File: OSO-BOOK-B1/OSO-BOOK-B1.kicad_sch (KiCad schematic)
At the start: 73 parts, among them J1 USB_C_Receptacle_USB2.0, J2 Conn_01x02_MountingPin, J3 Conn_01x24, J4 Conn_01x06, J5 JST-PH3, J6 JST-PH4, J7 JST-PH3, J8 Conn_ARM_JTAG_SWD_10, Q1 DMG3415, Q2 Q_PMOS_GSD, Q3 Q_NMOS_GSD, U1 XC6220B331MR-G, U2 ESP32-S3-WROOM-1, U3 MEM2075, U4 MCP73831-2-OT, U5 R1218, Y1 32.768 kHz

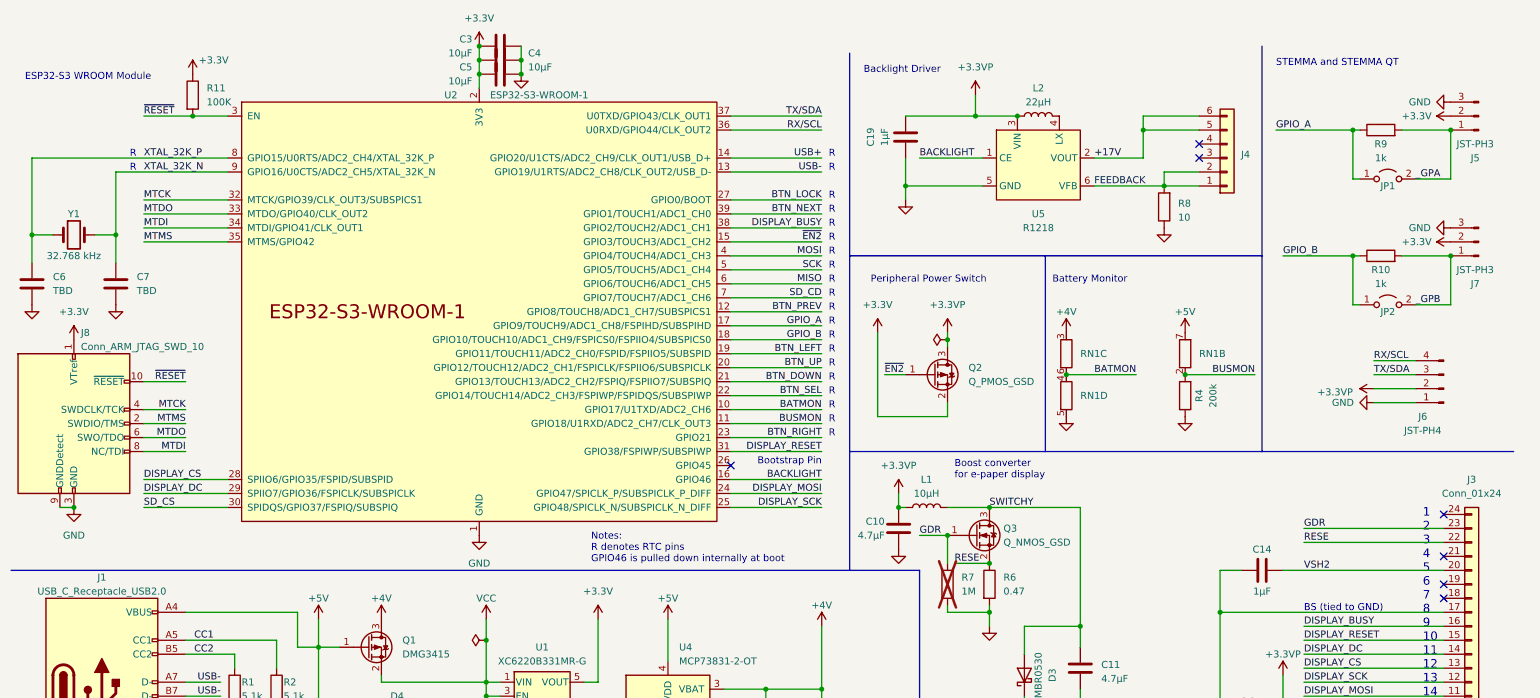
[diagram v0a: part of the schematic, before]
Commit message: Use surface mount push buttons
These buttons are basic parts at JLCPCB, so really inexpensive to use (1
cent per part, no setup fee).  They can then be covered by a silicone
cover for moisture protection and good looks.  Or even a 3d printed
cover can do the trick.
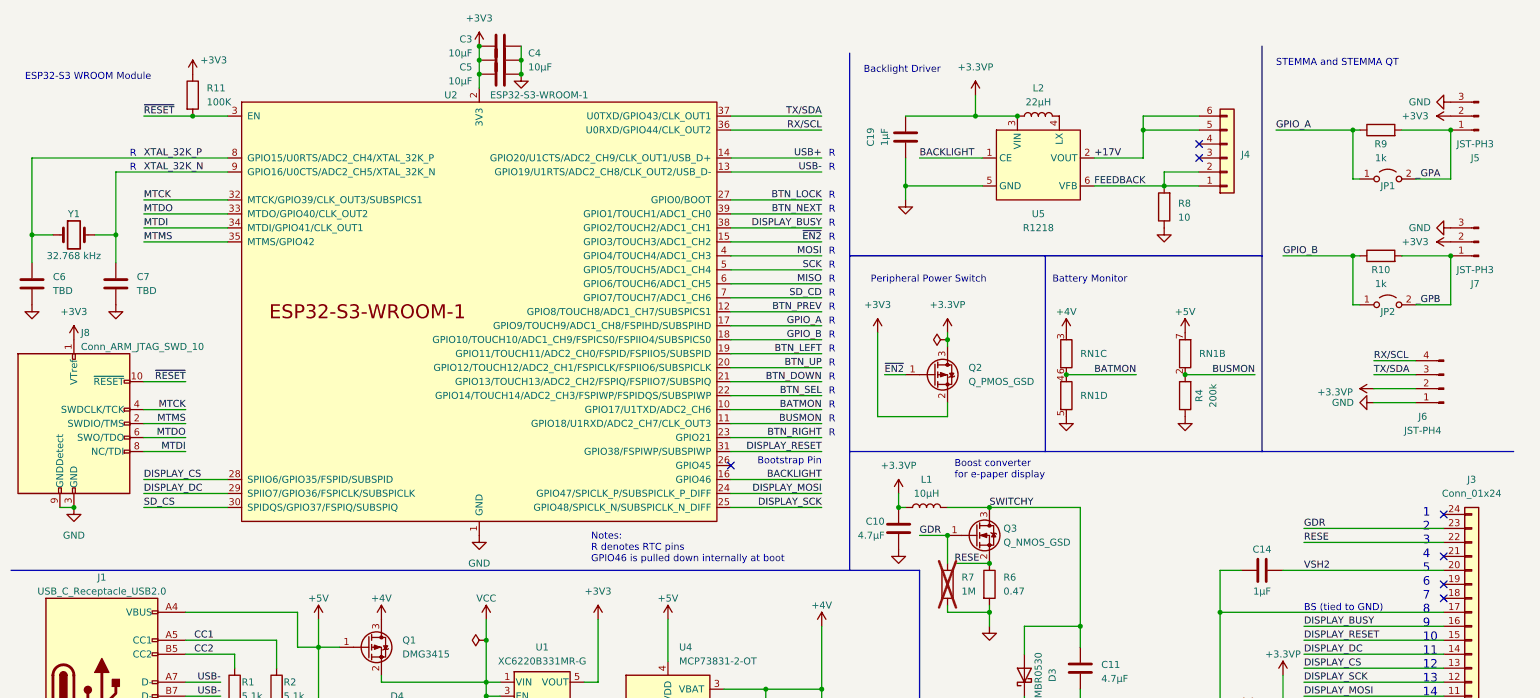
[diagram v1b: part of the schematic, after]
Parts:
- B3, B4, B5, B6, B7, B8, B9: footprint TACT_PANA-EVQ:TACT_PANA-EVQ-BUTTONPAD -> Button_Switch_SMD:SW_Push_1P1T_XKB_TS-1187A; JLCPCB (none) -> C318884
- U2: JLCPCB (none) -> C473012

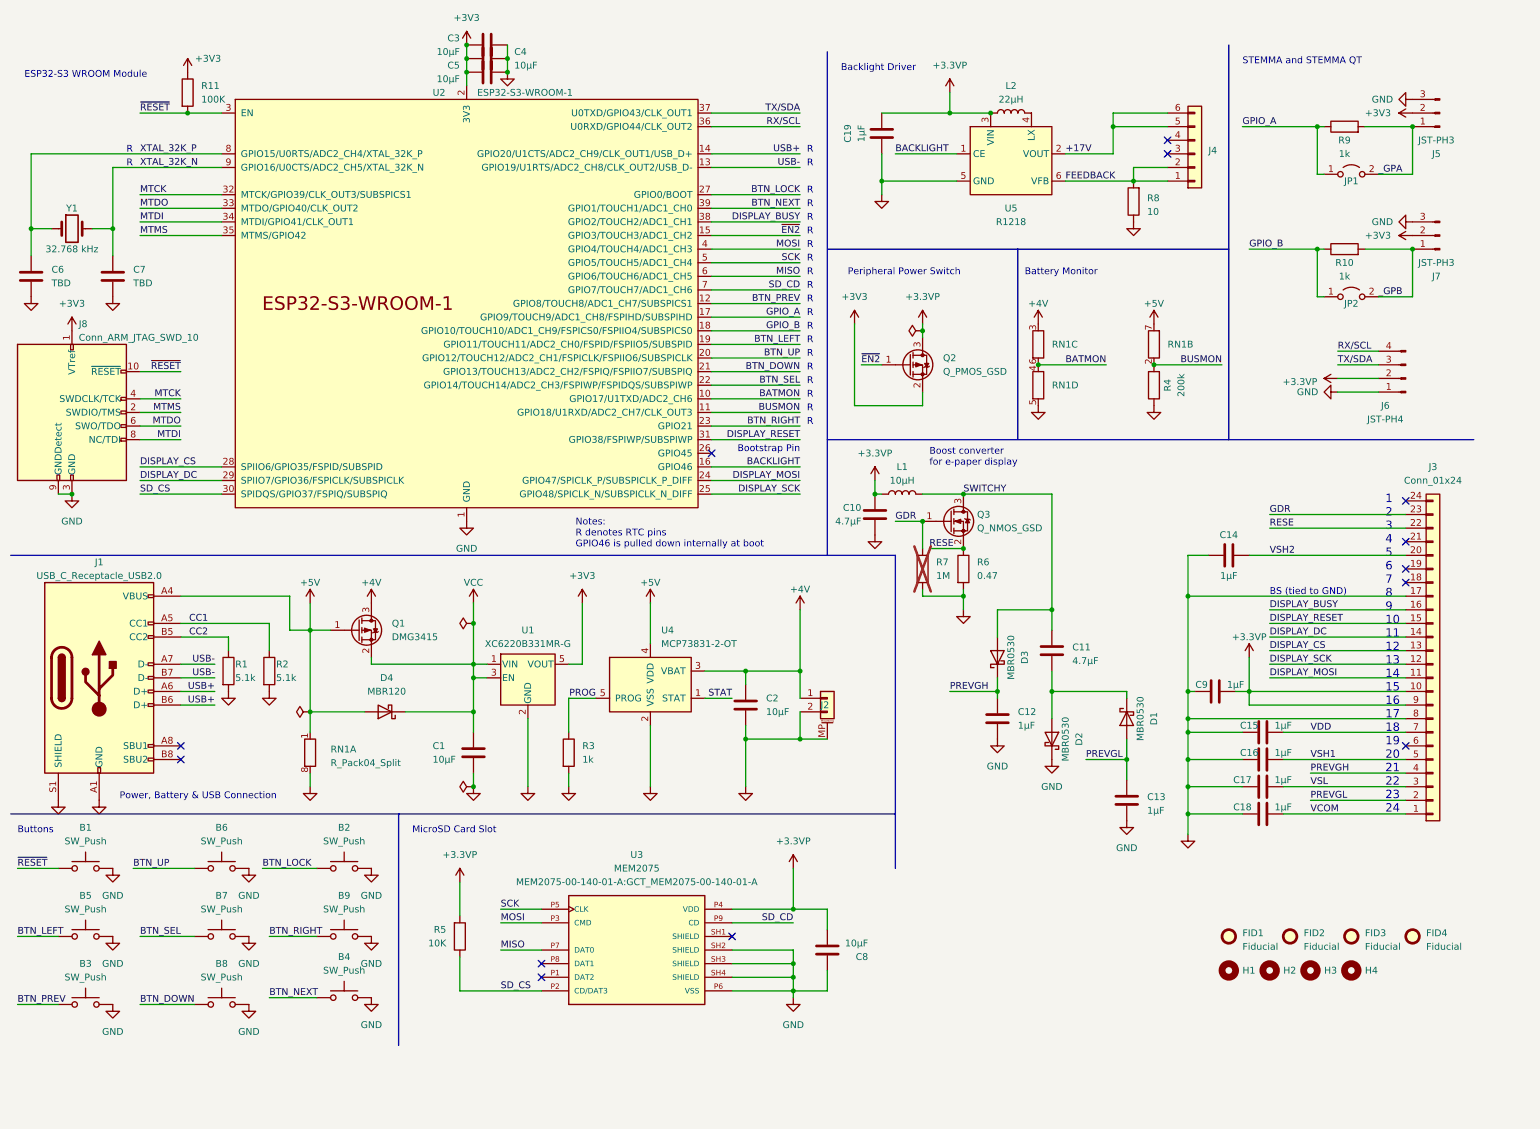
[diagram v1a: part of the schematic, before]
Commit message: Switch some parts
 - Pick a different SD-Card that is widely available
 - Use JLCPCB basic parts when possible
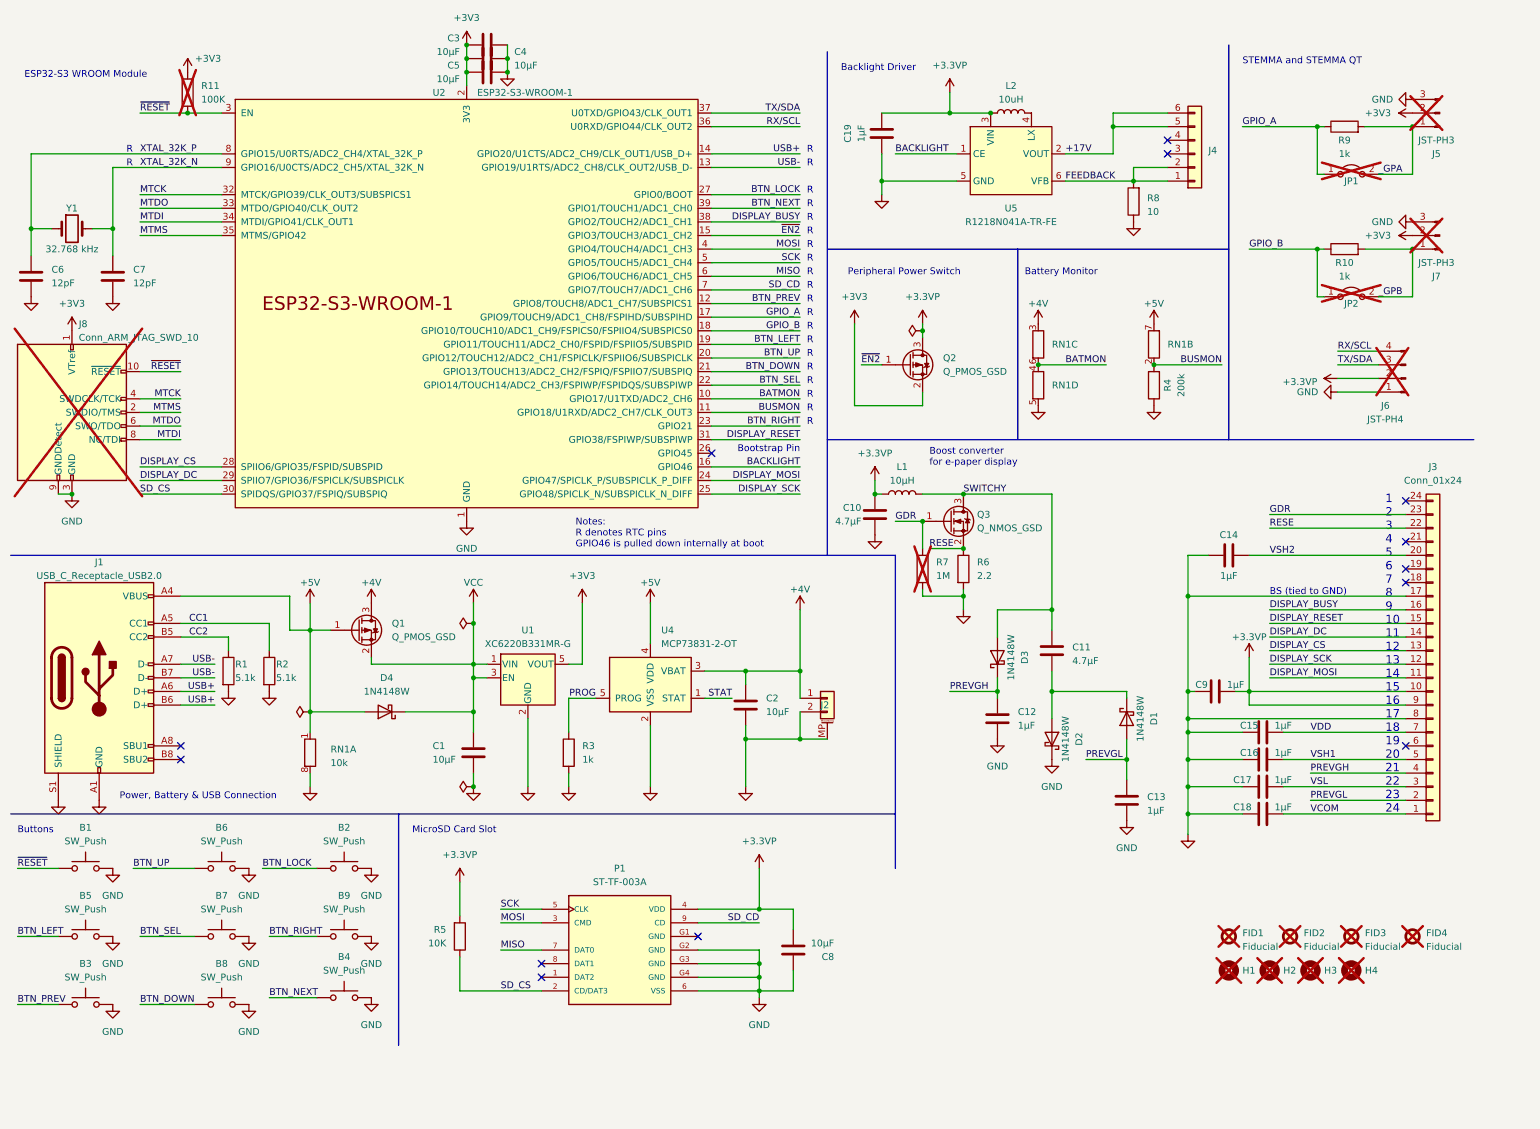
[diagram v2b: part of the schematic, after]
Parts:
- removed U3: MEM2075, MEM2075-00-140-01-A:GCT_MEM2075-00-140-01-A, symbol MEM2075-00-140-01-A:MEM2075-00-140-01-A
- added P1: ST-TF-003A, TF-CARD:SUNTECH_ST-TF-003A, symbol TF-CARD:ST-TF-003A
- B1, B2: JLCPCB (none) -> C128539
- C1, C2, C3, C4, C5, C8: JLCPCB (none) -> C13585
- C10, C11: JLCPCB (none) -> C1779
- C12, C13, C14, C15, C16, C17, C18, C19, C9: JLCPCB (none) -> C28323
- C6, C7: value TBD -> 12pF; footprint Capacitor_SMD:C_0805_2012Metric -> Capacitor_SMD:C_0603_1608Metric; JLCPCB (none) -> C38523
- D1, D2, D3: value MBR0530 -> 1N4148W; JLCPCB (none) -> C81598
- D4: value MBR120 -> 1N4148W; JLCPCB (none) -> C81598
- FID1, FID2, FID3, FID4, H1, H2, H3, H4, J5, J6, J7, J8, JP1, JP2, R11: now not fitted
- J1: JLCPCB (none) -> C165948
- J2: JLCPCB (none) -> C177225
- J3: JLCPCB (none) -> C262683
- J4: JLCPCB (none) -> C7465444
- L1: footprint Inductor_SMD:L_Taiyo-Yuden_MD-4040 -> Inductor_SMD:L_0805_2012Metric; JLCPCB (none) -> C1046
- L2: value 22µH -> 10uH; footprint Inductor_SMD:L_1210_3225Metric -> Inductor_SMD:L_0805_2012Metric; JLCPCB (none) -> C1046
- Q1: value DMG3415 -> Q_PMOS_GSD; JLCPCB (none) -> C15127
- Q2: JLCPCB (none) -> C15127
- Q3: JLCPCB (none) -> C8545
- R1, R2: JLCPCB (none) -> C27834
- R10, R3, R9: JLCPCB (none) -> C17513
- R4: JLCPCB (none) -> C17539
- R5: JLCPCB (none) -> C17414
- R6: value 0.47 -> 2.2; JLCPCB (none) -> C17521
- R8: JLCPCB (none) -> C17415
- RN1: value R_Pack04_Split -> 10k; JLCPCB (none) -> C29718
- U1: JLCPCB (none) -> C86534
- U4: JLCPCB (none) -> C424093
- U5: value R1218 -> R1218N041A-TR-FE; JLCPCB (none) -> C6749144
- Y1: JLCPCB (none) -> C32346
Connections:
- net +3.3VP: now also P1.4 (VDD)
- net GND: now also P1.6 (VSS), P1.G2 (GND), P1.G3 (GND), P1.G4 (GND)
- net MISO: now also P1.7 (DAT0)
- net MOSI: now also P1.3 (CMD)
- net SCK: now also P1.5 (CLK)
- net SD_CD: now also P1.9 (CD)
- net SD_CS: now also P1.2 (CD/DAT3)
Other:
- moved on the sheet: C8

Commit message: Packing script
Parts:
- FID1, FID2, FID3, FID4, R11: now left out of the parts list
- P1: JLCPCB (none) -> C393941
- R7: JLCPCB (none) -> C4310; now fitted

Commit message: More work on the buttons: rubber or SMD option
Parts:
- B3, B4, B5, B6, B7, B8, B9: footprint Button_Switch_SMD:SW_Push_1P1T_XKB_TS-1187A -> Keypad:SW_Push_1P1T_XKB_TS-1187A-Silicon-Hybrid
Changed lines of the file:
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@@
 			)
 		)
-		(property "Footprint" "Button_Switch_SMD:SW_Push_1P1T_XKB_TS-1187A"
+		(property "Footprint" "Keypad:SW_Push_1P1T_XKB_TS-1187A-Silicon-Hybrid"
 			(at 52.07 172.72 0)
 			(effects
@@
 			)
 		)
-		(property "Footprint" "Button_Switch_SMD:SW_Push_1P1T_XKB_TS-1187A"
+		(property "Footprint" "Keypad:SW_Push_1P1T_XKB_TS-1187A-Silicon-Hybrid"
 			(at 74.93 172.72 0)
 			(effects
@@
 			)
 		)
-		(property "Footprint" "Button_Switch_SMD:SW_Push_1P1T_XKB_TS-1187A"
+		(property "Footprint" "Keypad:SW_Push_1P1T_XKB_TS-1187A-Silicon-Hybrid"
 			(at 52.07 185.42 0)
 			(effects
@@
 			)
 		)
-		(property "Footprint" "Button_Switch_SMD:SW_Push_1P1T_XKB_TS-1187A"
+		(property "Footprint" "Keypad:SW_Push_1P1T_XKB_TS-1187A-Silicon-Hybrid"
 			(at 26.67 185.42 0)
 			(effects
@@
 			)
 		)
-		(property "Footprint" "Button_Switch_SMD:SW_Push_1P1T_XKB_TS-1187A"
+		(property "Footprint" "Keypad:SW_Push_1P1T_XKB_TS-1187A-Silicon-Hybrid"
 			(at 26.67 172.72 0)
 			(effects
@@
 			)
 		)
-		(property "Footprint" "Button_Switch_SMD:SW_Push_1P1T_XKB_TS-1187A"
+		(property "Footprint" "Keypad:SW_Push_1P1T_XKB_TS-1187A-Silicon-Hybrid"
 			(at 74.93 184.15 0)
 			(effects
@@
 			)
 		)
-		(property "Footprint" "Button_Switch_SMD:SW_Push_1P1T_XKB_TS-1187A"
+		(property "Footprint" "Keypad:SW_Push_1P1T_XKB_TS-1187A-Silicon-Hybrid"
 			(at 52.07 160.02 0)
 			(effects

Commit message: Use correct JLCPCB part number for ESP32-S3 module
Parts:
- U2: JLCPCB C473012 -> C2913198
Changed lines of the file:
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@@
 			)
 		)
-		(property "JLCPCB" "C473012"
+		(property "JLCPCB" "C2913198"
 			(at 97.79 59.69 0)
 			(effects

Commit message: Pick alternate part for bat connector
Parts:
- J2: Alternate (none) -> C177225; JLCPCB C177225 -> C225111
- J5, J6, J7, JP2: now left out of the parts list
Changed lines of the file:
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@@
 		(unit 1)
 		(exclude_from_sim no)
-		(in_bom yes)
+		(in_bom no)
 		(on_board yes)
 		(dnp yes)
@@
 			)
 		)
-		(property "JLCPCB" "C177225"
+		(property "JLCPCB" "C225111"
 			(at 165.1 133.35 0)
 			(effects
@@
 			)
 		)
+		(property "Alternate" "C177225"
+			(at 165.1 133.35 0)
+			(effects
+				(font
+					(size 1.27 1.27)
+				)
+				(hide yes)
+			)
+		)
 		(pin "1"
 		)
@@
 		(unit 1)
 		(exclude_from_sim no)
-		(in_bom yes)
+		(in_bom no)
 		(on_board yes)
 		(dnp yes)
@@
 		(unit 1)
 		(exclude_from_sim no)
-		(in_bom yes)
+		(in_bom no)
 		(on_board yes)
 		(dnp yes)
@@
 		(unit 1)
 		(exclude_from_sim no)
-		(in_bom yes)
+		(in_bom no)
 		(on_board yes)
 		(dnp yes)
